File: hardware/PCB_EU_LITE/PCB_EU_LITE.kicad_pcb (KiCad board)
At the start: 4 copper layers, 100 x 100 mm, 167 parts, among them J101 24 V IN, J201 UART 3V3, J301 MEM2061 SPI, J401 SHT4x XH2.54-4P-90, J403 FLOAT / GND, J411 FAN1 2510-4P 90deg, J421 FAN2 2510-4P 90deg, J501 LED + / GND, J502 LED 2 + / GND, J503 LED 3 + / GND, J701 PTC + / RETURN, J702 PUMP + / RETURN, Q102 IRL2505, Q411 FAN1 AO3422, Q421 FAN2 AO3422, Q501 BSC146N10LS5, Q701 BC847B-DIO, Q702 BC857B, Q703 CSD19531KCS, Q704 AO3422, Q901 BC847B (R), Q902 BC847B (G), Q903 BC847B (B), SW201 RESET, SW202 BOOT, U101 ST1S14PHR, U102 INA238, U201 ST1S10PHR, U202 ESP32-WROOM-32E-N4, U301 MCP7940N, U401 USBLC6-2SC6, U501 LM3429MH/NOPB, Y301 32.768k CL7p

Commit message: Apply the 283 kHz LED transition to sources, model and docs
Set R507 to 82k and R506 to 1k in the generator, regenerate the schematic,
design.json and BOM, and carry the new operating point (283.45 kHz,
1.444 A, 69.3 W) through verify.py, the power-stage model and the docs.
Only the Value fields of R506/R507 change on the board; geometry, nets and
silkscreen are untouched.

The procurement blocker is resolved: 82k is already in the 2026-10-23
catalogue snapshot and is now bought twice (R101 + R507); the 1k 1206 line
is added from the Salvats product page read on 2026-10-27 and preserved on
refresh through snapshot_prices.SITE_QUOTES. Purchase total is unchanged at
38.49 EUR with no unpriced lines.

verify.py (58 checks), its mutation tests, the boost-model tests, the price
refresh test, check_schematics.py and check_standalone.py pass. KiCad DRC,
board parity, fabricate.py and a new Gerber set were NOT run: no pcbnew,
Shapely or gerbonara in this environment. Gerber r3 stays historical and the
bench programme is still open.

Co-Authored-By: Claude Opus 5 <noreply@anthropic.com>
Claude-Session: https://claude.ai/code/session_01YbDYdPzNZ5NsoW89vkngV3
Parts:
- R506: value 620R 1% -> 1k 1%
- R507: value 56k 1% -> 82k 1%
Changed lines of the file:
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@@
 			)
 		)
-		(property "Value" "620R 1%"
+		(property "Value" "1k 1%"
 			(at 0 1.83 0)
 			(layer "F.Fab")
@@
 			)
 		)
-		(property "Value" "56k 1%"
+		(property "Value" "82k 1%"
 			(at 0 1.83 0)
 			(layer "F.Fab")

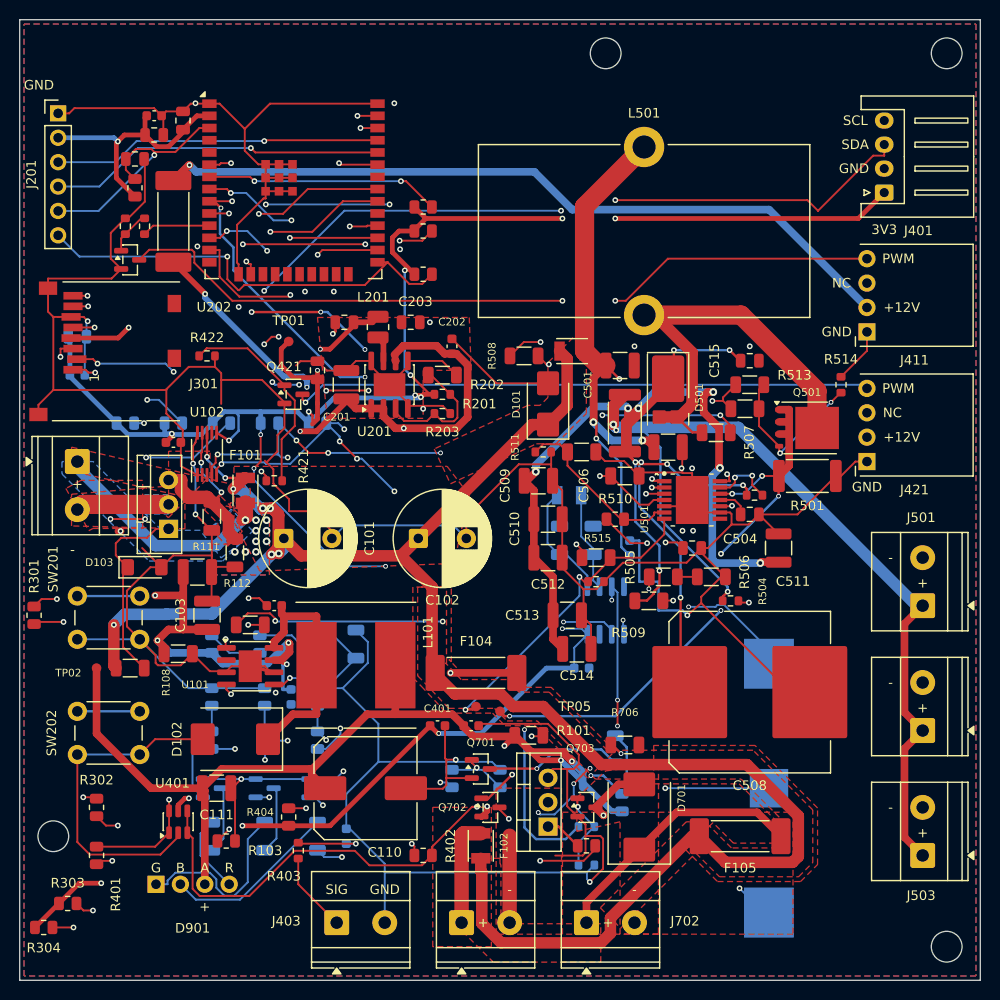
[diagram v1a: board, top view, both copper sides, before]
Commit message: Stitch the shunt ground and tighten the LED commutation loop
The GND pads of the INA238 shunts R111/R112 had no via to the inner
ground plane, so the whole return current climbed to F.Cu through a
SW201 pin and narrow pour necks (up to 33 A/mm in a DC model). Add 19
GND vias at the shunts and across their F.Cu ground island.

Rebuild the LED boost cell: D501 sits on the Q501 drain, C515 and two
4.7 uF capacitors (C514/C513 moved from the end of the output column)
run from the D501 cathode to a local ground shared with R501, the
inductor feed reaches the switch node from outside the loop, and the
gate resistors move under Q501. Give C508 a 1 mm feed instead of the
0.25 mm trace, and sync the R505/R506/R507 board fields with the
schematic. Schematic, nets and BOM are unchanged.

tools/repair_return_led_loop.py applies the change; placement.json
follows the moved footprints and silkscreen.py regenerated the labels.

Co-Authored-By: Claude Opus 5.5 <noreply@anthropic.com>
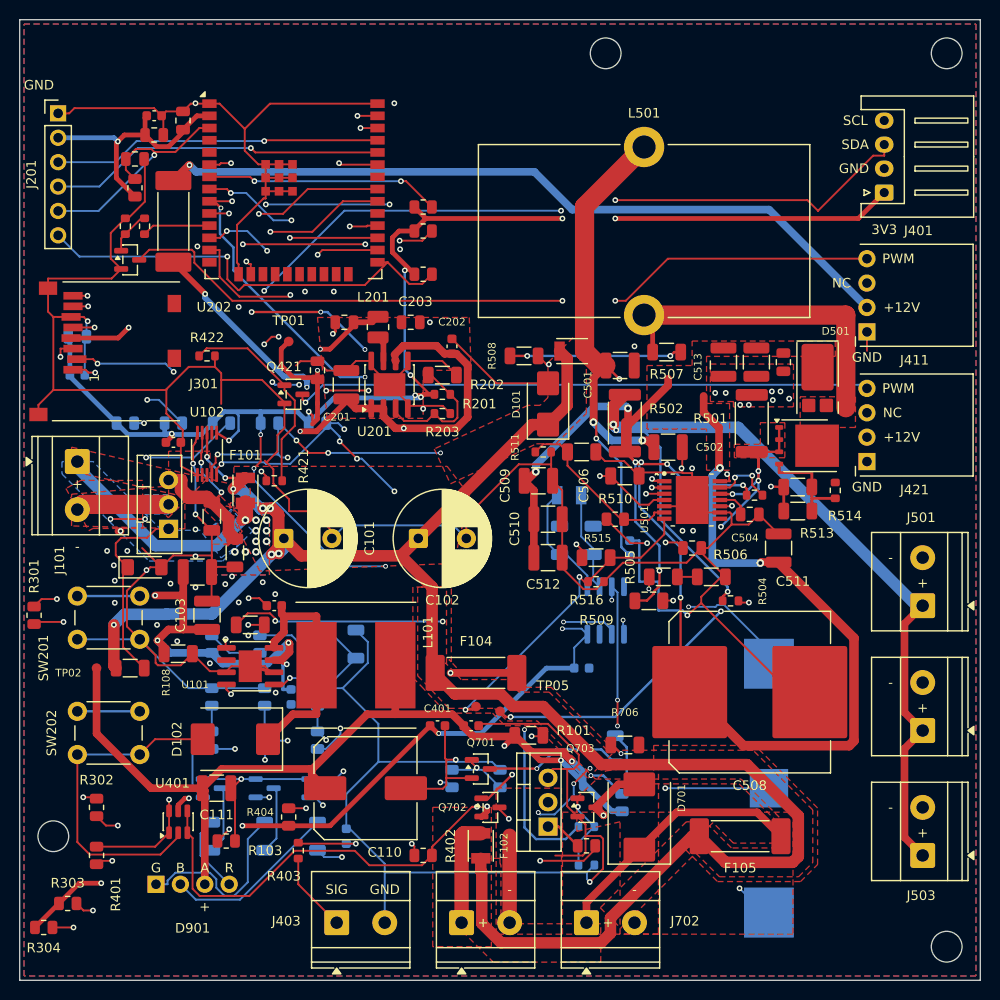
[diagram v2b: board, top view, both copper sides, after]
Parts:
- moved C514 35.2 mm to (76.7, 35.6), turned to -90 degrees
- moved C513 31.0 mm to (73.3, 35.6), turned to -90 degrees
- moved D501 15.6 mm to (83.1, 37.3)
- moved R513 14.1 mm to (81.0, 51.1)
- moved R514 11.0 mm to (84.9, 49.0)
- moved R507 9.85 mm to (67.3, 34.6)
- moved R512 9.83 mm to (81.0, 48.6)
- moved R501 7.97 mm to (76.2, 42.0), turned to 90 degrees
- moved C515 3.50 mm to (79.5, 35.6), turned to -90 degrees
- moved Q501 1.85 mm to (82.0, 44.4)
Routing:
- net GND: track 731.9 -> 707.9 mm, vias 25 -> 51
- net LED_SW: track 44.5 -> 32.0 mm
- net LED_RT_MID: track 28.6 -> 17.9 mm, vias 3 -> 2
- net LED_OUT: track 160.6 -> 169.1 mm, vias 14 -> 10
- net LED_GATE: track 17.2 -> 10.7 mm, vias 2 -> 0
- net LED_IS: track 61.7 -> 59.7 mm
- net LED_GATE_RAW: track 17.5 -> 19.4 mm
- added copper zone on F.Cu, net LED_IS
- added copper zone on F.Cu, net LED_OUT
- added copper zone on F.Cu, net LED_SW
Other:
- board text added: "C502"
- board text added: "J101"
- board text added: "R502"
- board text added: "R516"
- board text removed: "C514"
- board text removed: "C515"
- board text removed: "D103"
- board text removed: "Q501"
- board text removed: "R111"
- board text removed: "R112"

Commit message: Route the C508 feed away from its exposed GND pad
The 1 mm C508 feed from r4 ran under the capacitor body along the
exposed C508.2 GND pad at the 0.2 mm minimum, with up to ~55 V across.
Lay it explicitly on F.Cu from C511.1, down between the R506 pads and
into C508.1 from its own side, 5.85 mm from the GND pad; the script now
refuses a feed closer than 0.5 mm.

Remove six thin F.Cu GND ties inside the ground pour that blocked the
path (one of them ran under C508 to its GND pad). R506.2, the CSH set
resistor ground, gets a solid pour connection and its own plane via.

Co-Authored-By: Claude Opus 5.5 <noreply@anthropic.com>
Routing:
- net LED_OUT: track 169.1 -> 144.3 mm
- net GND: track 707.9 -> 684.9 mm, vias 51 -> 52
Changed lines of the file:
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@@
 			(roundrect_rratio 0.222222)
 			(net "GND")
+			(zone_connect 2)
 		)
 		(embedded_fonts no)
@@
 	)
 	(segment
-		(start 80.2183 70)
-		(end 70.9489 60.7306)
-		(width 0.2)
-		(layer "F.Cu")
-		(net "GND")
-	)
-	(segment
 		(start 40.405 35.525)
 		(end 40.405 36.095)
@@
 	)
 	(segment
-		(start 73.0221 58)
-		(end 73.4625 58)
-		(width 0.2)
-		(layer "F.Cu")
-		(net "GND")
-	)
-	(segment
 		(start 64.8397 47.1353)
 		(end 68.975 47.1353)
@@
 	)
 	(segment
-		(start 73.4625 58)
-		(end 70.7063 55.2437)
-		(width 0.2)
-		(layer "F.Cu")
-		(net "GND")
-	)
-	(segment
 		(start 20 55.776)
 		(end 20 56.45)
@@
 	)
 	(segment
-		(start 70.9489 60.7306)
-		(end 70.9489 60.0732)
-		(width 0.2)
-		(layer "F.Cu")
-		(net "GND")
-	)
-	(segment
 		(start 23.4284 13.6401)
 		(end 24.8483 15.06)
@@
 	)
 	(segment
-		(start 70.95 60.73)
-		(end 69.5 62)
-		(width 0.2)
-		(layer "F.Cu")
-		(net "GND")
-	)
-	(segment
 		(start 43.9875 35.525)
 		(end 40.405 35.525)
@@
 		(net "GND")
 	)
-	(segment
-		(start 70.9489 60.0732)
-		(end 73.0221 58)
-		(width 0.2)
-		(layer "F.Cu")
-		(net "GND")
-	)
 	(via
 		(at 21.4 58.76)
@@
 	)
 	(via
+		(at 74.8 58)
+		(size 0.6)
+		(drill 0.3)
+		(layers "F.Cu" "B.Cu")
+		(net "GND")
+	)
+	(via
 		(at 13.2 57.3)
 		(size 0.6)
@@
 	)
 	(segment
-		(start 86.35 75.575)
-		(end 75.35 75.575)
-		(width 1)
-		(layer "F.Cu")
-		(net "LED_OUT")
-	)
-	(segment
 		(start 63 44.9625)
 		(end 64.099999 46.0625)
@@
 	)
 	(segment
-		(start 75.35 75.575)
-		(end 69.75 69.975)
-		(width 1)
-		(layer "F.Cu")
-		(net "LED_OUT")
-	)
-	(segment
 		(start 66 59.6625)
 		(end 66 59.7625)
@@
 	)
 	(segment
-		(start 86.85 75.075)
-		(end 86.35 75.575)
-		(width 1)
-		(layer "F.Cu")
-		(net "LED_OUT")
-	)
-	(segment
 		(start 52.525 48)
 		(end 53.525 49)
@@
 	)
 	(segment
-		(start 69.75 69.975)
-		(end 69.75 70)
-		(width 1)
-		(layer "F.Cu")
-		(net "LED_OUT")
-	)
-	(segment
-		(start 86.85 64.375)
-		(end 86.85 75.075)
-		(width 1)
-		(layer "F.Cu")
-		(net "LED_OUT")
-	)
-	(segment
 		(start 67.5 37.374)
 		(end 67.5 37.4)
@@
 	)
 	(segment
-		(start 78.95 56.475)
-		(end 86.85 64.375)
-		(width 1)
-		(layer "F.Cu")
-		(net "LED_OUT")
-	)
-	(segment
 		(start 64.3 46.2625)
 		(end 67.4 46.2625)
@@
 	)
 	(segment
+		(start 79 56.3)
+		(end 72 56.3)
+		(width 1)
+		(layer "F.Cu")
+		(net "LED_OUT")
+	)
+	(segment
 		(start 63 44.9625)
 		(end 63.025 44.9625)
@@
 	)
 	(segment
-		(start 79 56.475)
-		(end 78.95 56.475)
-		(width 1)
-		(layer "F.Cu")
-		(net "LED_OUT")
-	)
-	(segment
 		(start 75.3 48.4625)
 		(end 75.7 48.8625)
@@
 		(layer "F.Cu")
 		(net "LED_OUT")
+	)
+	(segment
+		(start 72 56.3)
+		(end 72 66)
+		(width 1)
+		(layer "F.Cu")
+		(net "LED_OUT")
